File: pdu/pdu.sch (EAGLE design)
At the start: 3 parts

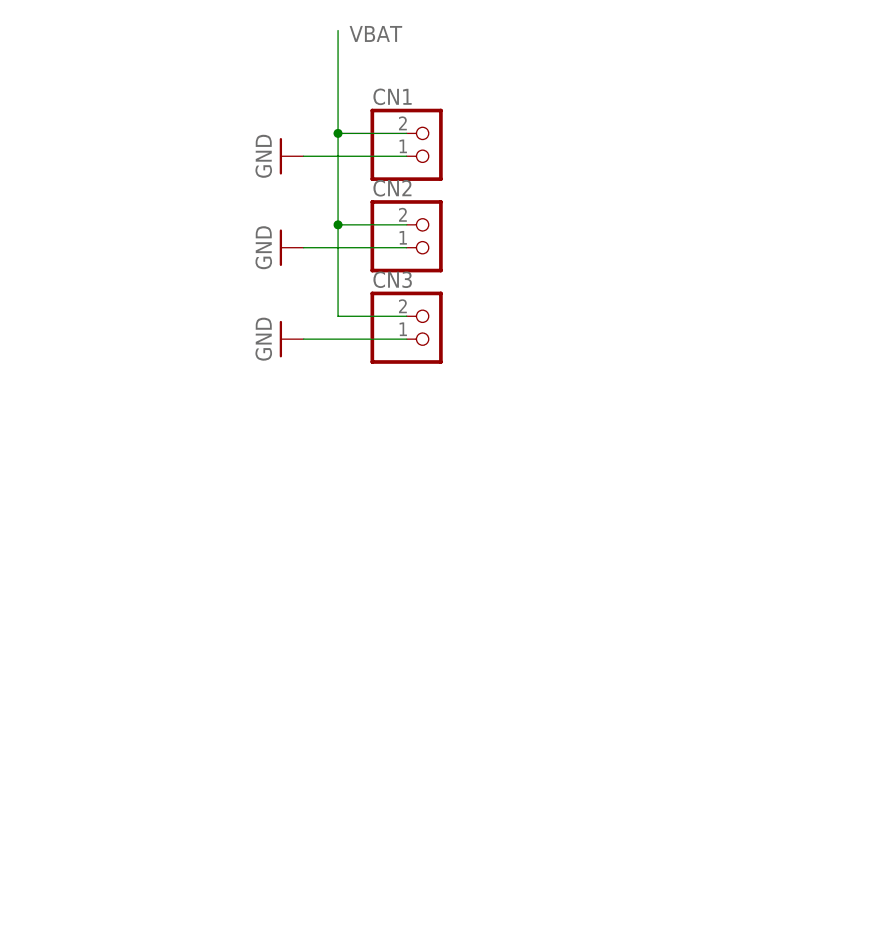
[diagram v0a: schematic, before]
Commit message: initial mosfet with RC
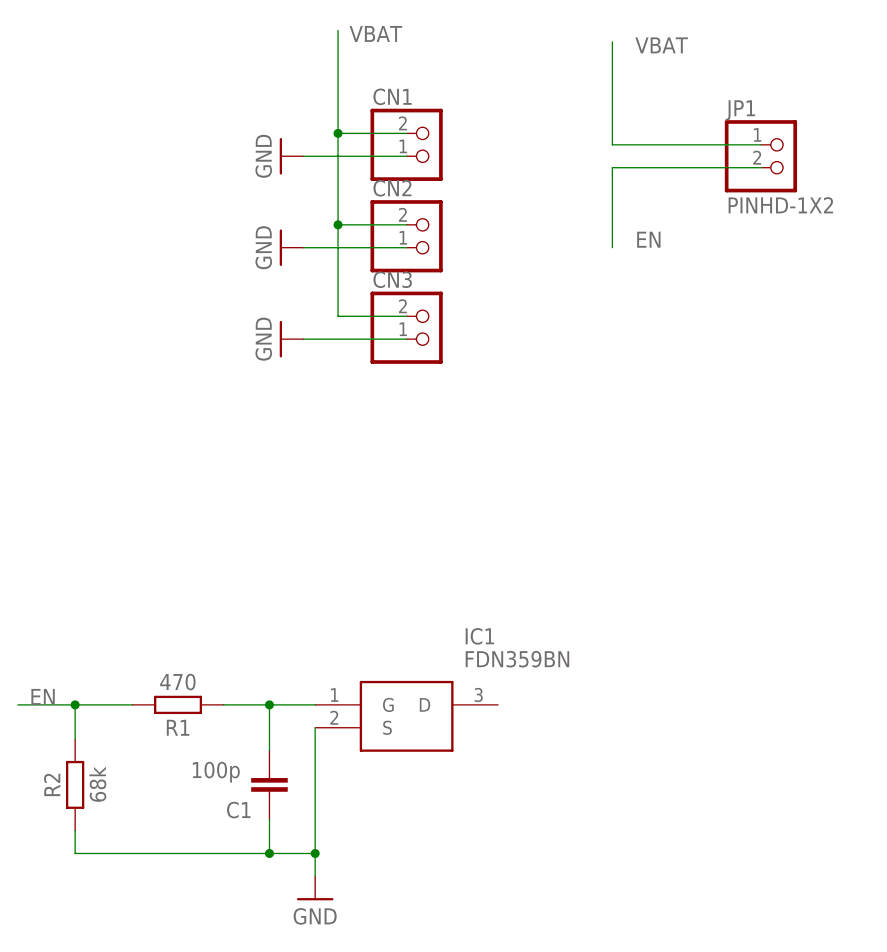
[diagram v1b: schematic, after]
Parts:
- added C1: 100p, Capacitor:C_CHIP-0603(1608-METRIC)
- added IC1: FDN359BN, SamacSys_Parts:FDN359BN
- added JP1: PINHD-1X2, Connector:PINHD-1X2
- added R1: 470, Resistor:R_CHIP-0603(1608-METRIC)
- added R2: 68k, Resistor:R_CHIP-0603(1608-METRIC)
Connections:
- new net EN: JP1.2, R1.2, R2.2
- new net N$1: C1.2, IC1.G, R1.1
- net GND: now also C1.1, IC1.S, R2.1
- net VBAT: now also JP1.1

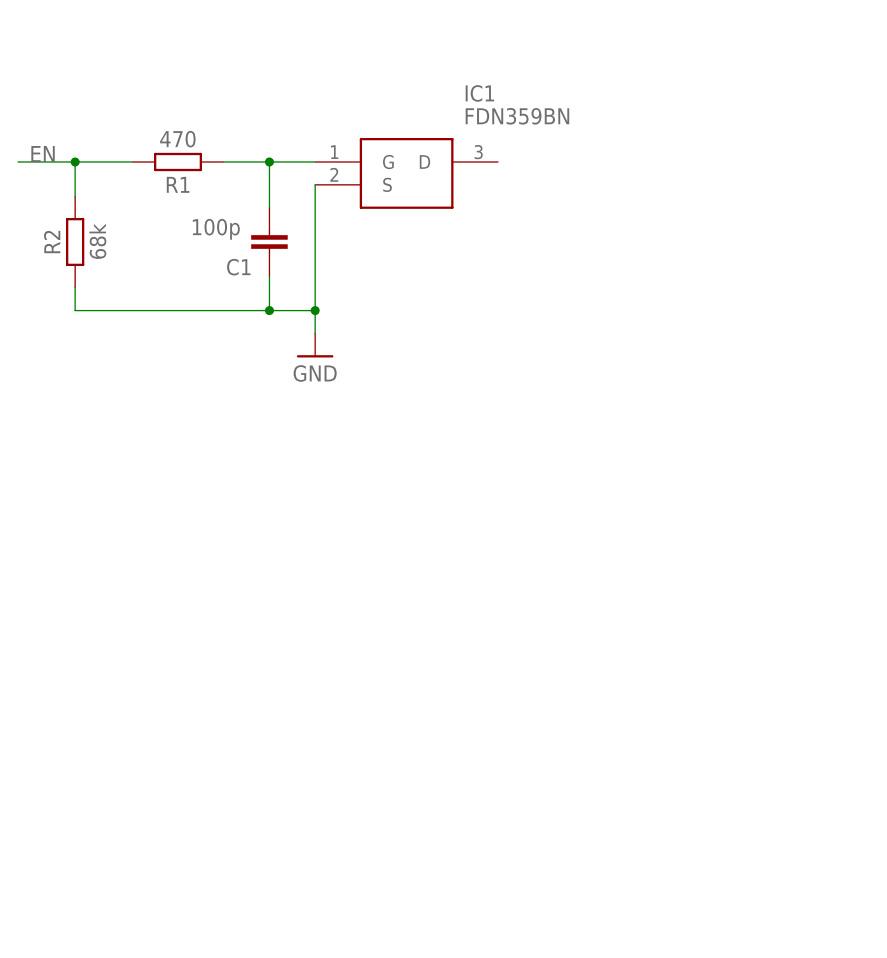
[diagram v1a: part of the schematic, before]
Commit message: parallel mosfets
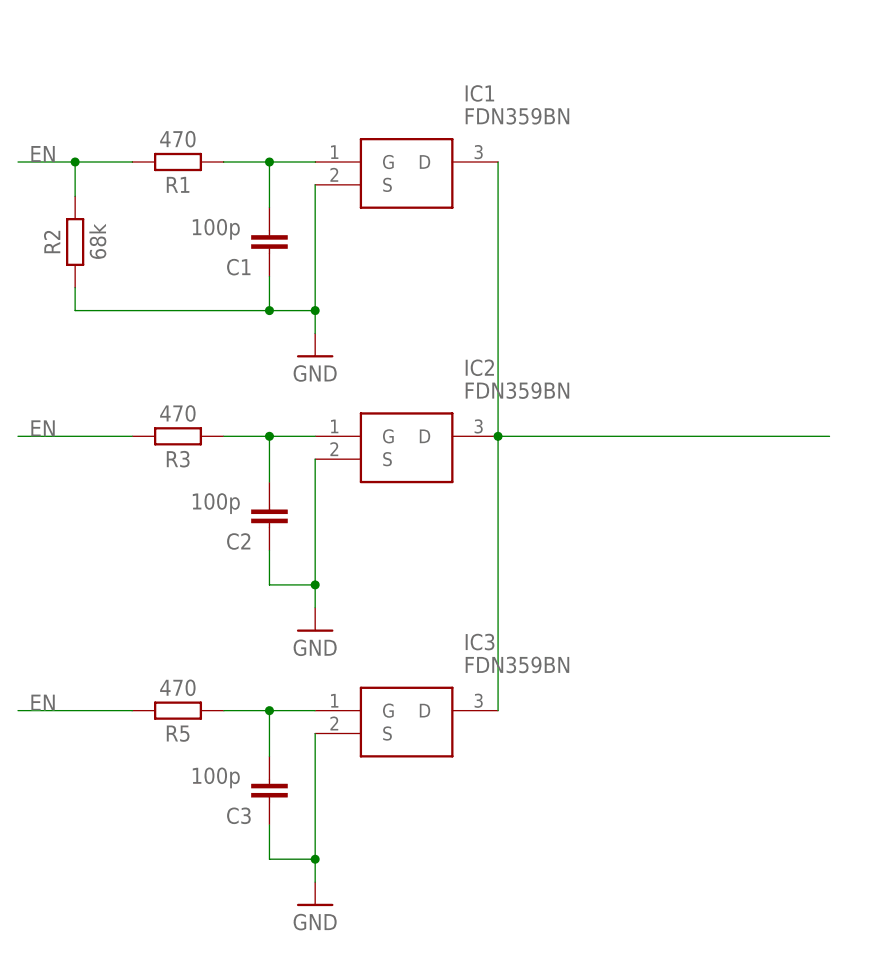
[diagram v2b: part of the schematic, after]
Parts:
- added C2, C3: 100p, Capacitor:C_CHIP-0603(1608-METRIC)
- added IC2, IC3: FDN359BN, SamacSys_Parts:FDN359BN
- added R3, R5: 470, Resistor:R_CHIP-0603(1608-METRIC)
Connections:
- new net N$2: C2.2, IC2.G, R3.1
- new net N$3: C3.2, IC3.G, R5.1
- new net N$4: IC1.D, IC2.D, IC3.D
- net EN: now also R3.2, R5.2
- net GND: now also C2.1, C3.1, IC2.S, IC3.S
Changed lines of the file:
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@@
 <part name="SUPPLY4" library="Power_Symbols" library_urn="urn:adsk.eagle:library:16502351" deviceset="GND-BAR" device="" value="GND"/>
 <part name="C1" library="Capacitor" library_urn="urn:adsk.eagle:library:16290819" deviceset="C" device="CHIP-0603(1608-METRIC)" package3d_urn="urn:adsk.eagle:package:16290898/5" technology="_" value="100p"/>
+<part name="IC2" library="SamacSys_Parts" deviceset="FDN359BN" device=""/>
+<part name="R3" library="Resistor" library_urn="urn:adsk.eagle:library:16378527" deviceset="R" device="CHIP-0603(1608-METRIC)" package3d_urn="urn:adsk.eagle:package:16378565/5" technology="_" value="470"/>
+<part name="SUPPLY5" library="Power_Symbols" library_urn="urn:adsk.eagle:library:16502351" deviceset="GND-BAR" device="" value="GND"/>
+<part name="C2" library="Capacitor" library_urn="urn:adsk.eagle:library:16290819" deviceset="C" device="CHIP-0603(1608-METRIC)" package3d_urn="urn:adsk.eagle:package:16290898/5" technology="_" value="100p"/>
+<part name="IC3" library="SamacSys_Parts" deviceset="FDN359BN" device=""/>
+<part name="R5" library="Resistor" library_urn="urn:adsk.eagle:library:16378527" deviceset="R" device="CHIP-0603(1608-METRIC)" package3d_urn="urn:adsk.eagle:package:16378565/5" technology="_" value="470"/>
+<part name="SUPPLY6" library="Power_Symbols" library_urn="urn:adsk.eagle:library:16502351" deviceset="GND-BAR" device="" value="GND"/>
+<part name="C3" library="Capacitor" library_urn="urn:adsk.eagle:library:16290819" deviceset="C" device="CHIP-0603(1608-METRIC)" package3d_urn="urn:adsk.eagle:package:16290898/5" technology="_" value="100p"/>
 </parts>
 <sheets>
@@
 <attribute name="NAME" x="-6.985" y="-10.795" size="1.778" layer="95" rot="R180"/>
 <attribute name="VALUE" x="-8.255" y="-6.35" size="1.778" layer="96" rot="R180"/>
+</instance>
+<instance part="IC2" gate="G$1" x="0" y="-30.48" smashed="yes">
+<attribute name="NAME" x="16.51" y="-22.86" size="1.778" layer="95" align="center-left"/>
+<attribute name="VALUE" x="16.51" y="-25.4" size="1.778" layer="96" align="center-left"/>
+</instance>
+<instance part="R3" gate="G$1" x="-15.24" y="-30.48" smashed="yes" rot="R180">
+<attribute name="NAME" x="-15.24" y="-33.02" size="1.778" layer="95" rot="R180" align="center"/>
+<attribute name="VALUE" x="-15.24" y="-27.94" size="1.778" layer="96" rot="R180" align="center"/>
+</instance>
+<instance part="SUPPLY5" gate="G$1" x="0" y="-52.07" smashed="yes">
+<attribute name="VALUE" x="0" y="-53.975" size="1.778" layer="96" align="center"/>
+</instance>
+<instance part="C2" gate="G$1" x="-5.08" y="-40.64" smashed="yes" rot="R180">
+<attribute name="NAME" x="-6.985" y="-41.275" size="1.778" layer="95" rot="R180"/>
+<attribute name="VALUE" x="-8.255" y="-36.83" size="1.778" layer="96" rot="R180"/>
+</instance>
+<instance part="IC3" gate="G$1" x="0" y="-60.96" smashed="yes">
+<attribute name="NAME" x="16.51" y="-53.34" size="1.778" layer="95" align="center-left"/>
+<attribute name="VALUE" x="16.51" y="-55.88" size="1.778" layer="96" align="center-left"/>
+</instance>
+<instance part="R5" gate="G$1" x="-15.24" y="-60.96" smashed="yes" rot="R180">
+<attribute name="NAME" x="-15.24" y="-63.5" size="1.778" layer="95" rot="R180" align="center"/>
+<attribute name="VALUE" x="-15.24" y="-58.42" size="1.778" layer="96" rot="R180" align="center"/>
+</instance>
+<instance part="SUPPLY6" gate="G$1" x="0" y="-82.55" smashed="yes">
+<attribute name="VALUE" x="0" y="-84.455" size="1.778" layer="96" align="center"/>
+</instance>
+<instance part="C3" gate="G$1" x="-5.08" y="-71.12" smashed="yes" rot="R180">
+<attribute name="NAME" x="-6.985" y="-71.755" size="1.778" layer="95" rot="R180"/>
+<attribute name="VALUE" x="-8.255" y="-67.31" size="1.778" layer="96" rot="R180"/>
 </instance>
 </instances>
@@
 <junction x="-5.08" y="-16.51"/>
 </segment>
+<segment>
+<pinref part="SUPPLY5" gate="G$1" pin="GND"/>
+<pinref part="IC2" gate="G$1" pin="S"/>
+<wire x1="0" y1="-49.53" x2="0" y2="-46.99" width="0.1524" layer="91"/>
+<pinref part="C2" gate="G$1" pin="1"/>
+<wire x1="0" y1="-46.99" x2="0" y2="-33.02" width="0.1524" layer="91"/>
+<wire x1="-5.08" y1="-43.18" x2="-5.08" y2="-46.99" width="0.1524" layer="91"/>
+<wire x1="-5.08" y1="-46.99" x2="0" y2="-46.99" width="0.1524" layer="91"/>
+<junction x="0" y="-46.99"/>
+</segment>
+<segment>
+<pinref part="SUPPLY6" gate="G$1" pin="GND"/>
+<pinref part="IC3" gate="G$1" pin="S"/>
+<wire x1="0" y1="-80.01" x2="0" y2="-77.47" width="0.1524" layer="91"/>
+<pinref part="C3" gate="G$1" pin="1"/>
+<wire x1="0" y1="-77.47" x2="0" y2="-63.5" width="0.1524" layer="91"/>
+<wire x1="-5.08" y1="-73.66" x2="-5.08" y2="-77.47" width="0.1524" layer="91"/>
+<wire x1="-5.08" y1="-77.47" x2="0" y2="-77.47" width="0.1524" layer="91"/>
+<junction x="0" y="-77.47"/>
+</segment>
 </net>
 <net name="VBAT" class="0">
@@
 <junction x="-26.67" y="0"/>
 </segment>
+<segment>
+<pinref part="R3" gate="G$1" pin="2"/>
+<label x="-31.75" y="-30.48" size="1.778" layer="95"/>
+<wire x1="-20.32" y1="-30.48" x2="-33.02" y2="-30.48" width="0.1524" layer="91"/>
+</segment>
+<segment>
+<pinref part="R5" gate="G$1" pin="2"/>
+<label x="-31.75" y="-60.96" size="1.778" layer="95"/>
+<wire x1="-20.32" y1="-60.96" x2="-33.02" y2="-60.96" width="0.1524" layer="91"/>
+</segment>
 </net>
 <net name="N$1" class="0">
@@
 </segment>
 </net>
+<net name="N$2" class="0">
+<segment>
+<pinref part="R3" gate="G$1" pin="1"/>
+<pinref part="IC2" gate="G$1" pin="G"/>
+<wire x1="-10.16" y1="-30.48" x2="-5.08" y2="-30.48" width="0.1524" layer="91"/>
+<pinref part="C2" gate="G$1" pin="2"/>
+<wire x1="-5.08" y1="-30.48" x2="0" y2="-30.48" width="0.1524" layer="91"/>
+<wire x1="-5.08" y1="-35.56" x2="-5.08" y2="-30.48" width="0.1524" layer="91"/>
+<junction x="-5.08" y="-30.48"/>
+</segment>
+</net>
+<net name="N$3" class="0">
+<segment>
+<pinref part="R5" gate="G$1" pin="1"/>
+<pinref part="IC3" gate="G$1" pin="G"/>
+<wire x1="-10.16" y1="-60.96" x2="-5.08" y2="-60.96" width="0.1524" layer="91"/>
+<pinref part="C3" gate="G$1" pin="2"/>
+<wire x1="-5.08" y1="-60.96" x2="0" y2="-60.96" width="0.1524" layer="91"/>
+<wire x1="-5.08" y1="-66.04" x2="-5.08" y2="-60.96" width="0.1524" layer="91"/>
+<junction x="-5.08" y="-60.96"/>
+</segment>
+</net>
+<net name="N$4" class="0">
+<segment>
+<pinref part="IC3" gate="G$1" pin="D"/>
+<pinref part="IC2" gate="G$1" pin="D"/>
+<wire x1="20.32" y1="-60.96" x2="20.32" y2="-30.48" width="0.1524" layer="91"/>
+<pinref part="IC1" gate="G$1" pin="D"/>
+<wire x1="20.32" y1="-30.48" x2="20.32" y2="0" width="0.1524" layer="91"/>
+<junction x="20.32" y="-30.48"/>
+<wire x1="20.32" y1="-30.48" x2="57.15" y2="-30.48" width="0.1524" layer="91"/>
+</segment>
+</net>
